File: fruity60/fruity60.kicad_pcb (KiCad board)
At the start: 2 copper layers, 126 parts

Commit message: progress
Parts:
- removed D0: D_Small, Diodes_SMD:D_SOD-123
- added De: D_Small, Diodes_SMD:D_SOD-123, F.Cu at (-67.5, 38.9)
- moved D1 7.94 mm to (-48.4, 38.9)
- moved D2 7.14 mm to (-29.4, 38.9)
- moved D3 7.14 mm to (-10.3, 38.9)
- moved D4 7.14 mm to (8.73, 38.9)
- moved D5 7.14 mm to (27.8, 38.9)
- moved D6 7.14 mm to (46.8, 38.9)
- moved D7 7.14 mm to (65.9, 38.9)
- moved D8 7.14 mm to (84.9, 38.9)
- moved D9 7.14 mm to (104.0, 38.9)
- moved DA1 7.14 mm to (123.0, 38.9)
- moved D10 5.62 mm to (-65.1, 42.1)
- moved D11 5.56 mm to (-46.0, 42.1)
- moved D12 5.56 mm to (-27.0, 42.1)
- moved D13 5.56 mm to (-7.94, 42.1)
- moved D14 5.56 mm to (11.1, 42.1)
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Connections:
- MX0A1 pad 1: B7 -> C7
- MX18 pad 1: C7 -> B7
- MX1A1 pad 1: B7 -> C7
- MX28 pad 1: C7 -> B7
- MX2A1 pad 1: B7 -> C7
- MX38 pad 1: C7 -> B7
- MX3A1 pad 1: B7 -> C7
- MX48 pad 1: C7 -> B7
- MX4A1 pad 1: B7 -> C7
- MX58 pad 1: C7 -> B7
- MX5A1 pad 1: B7 -> C7
- MX8 pad 1: C7 -> B7
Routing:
- net D3: track 197.3 -> 457.5 mm
- net D2: track 220.8 -> 438.2 mm
- net C6: track 239.4 -> 42.3 mm
- net F0: track 283.4 -> 464.0 mm
- net F1: track 277.0 -> 419.8 mm
- net Net-(D4A1-Pad2): track 0.00 -> 127.3 mm
- net Net-(D49-Pad2): track 0.00 -> 126.1 mm
- net Net-(D59-Pad2): track 0.00 -> 119.9 mm
- net Net-(D48-Pad2): track 0.00 -> 117.8 mm
- net Net-(D45-Pad2): track 0.00 -> 108.9 mm
- net Net-(D56-Pad2): track 0.00 -> 107.1 mm
- net Net-(D5A1-Pad2): track 0.00 -> 103.9 mm
- net Net-(D41-Pad2): track 0.00 -> 103.3 mm
- net F4: track 298.0 -> 400.2 mm
- net Net-(D42-Pad2): track 0.00 -> 95.5 mm
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
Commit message: 10 unconnected10 unconnected10 unconnected10 unconnected10 unconnected10 unconnected10 unconnected10 unconnected10 unconnected10 unconnected
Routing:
- net C6: track 42.3 -> 302.2 mm, vias 0 -> 11
- net D0: track 37.5 -> 257.8 mm, vias 0 -> 7
- net C7: track 151.6 -> 215.7 mm
- net D6: track 212.4 -> 233.1 mm
- net Net-(D45-Pad2): track 108.9 -> 94.8 mm
- net Net-(D57-Pad2): track 93.3 -> 79.2 mm
- net Net-(D35-Pad2): track 74.2 -> 76.1 mm
- net D7: track 301.4 -> 300.1 mm
- net F6: vias 2 -> 0

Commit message: Update with all nets
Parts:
- JP1: footprint Pin_Headers:Pin_Header_Straight_1x16_Pitch2.54mm -> Adafruit Feather 32u4 Bluefruit LE:1X16_ROUND
- JP2: footprint Pin_Headers:Pin_Header_Straight_1x12_Pitch2.54mm -> Adafruit Feather 32u4 Bluefruit LE:1X12_ROUND
- moved JP1 29.6 mm to (191.8, 25.4), turned to 0 degrees
- moved JP2 8.64 mm to (186.7, 45.7), turned to 180 degrees
- moved D1A1 8.59 mm to (132.6, 37.3)
- moved D49 8.59 mm to (120.7, 47.6)
- moved D50 8.59 mm to (144.5, 47.6)
- moved D51 8.59 mm to (146.8, 47.6)
- moved D54 8.59 mm to (154.0, 47.6)
- moved D55 8.59 mm to (156.4, 47.6)
- moved D56 8.59 mm to (158.8, 47.6)
- moved D59 8.59 mm to (165.9, 47.6)
- moved D5A1 8.59 mm to (168.3, 47.6)
- moved MX27 8.59 mm to (84.9, 98.4)
- moved MX2A1 8.59 mm to (142.1, 98.4)
- moved MX39 8.59 mm to (132.6, 117.5)
- moved MX50 8.59 mm to (146.8, 60.3)
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- renumbered De to D0
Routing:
- net D3: track 457.5 -> 610.9 mm, vias 0 -> 2
- net F1: track 419.8 -> 545.0 mm
- net B7: track 224.2 -> 334.0 mm, vias 0 -> 1
- net D2: track 438.2 -> 536.8 mm, vias 0 -> 2
- net F0: track 464.0 -> 552.2 mm
- net Net-(D58-Pad2): track 31.3 -> 118.5 mm, vias 1 -> 2
- net F6: track 395.1 -> 476.4 mm, vias 0 -> 1
- net F7: track 384.4 -> 445.4 mm
- net F4: track 400.2 -> 451.3 mm
- net F5: track 409.6 -> 428.9 mm, vias 0 -> 1

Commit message: first milestone
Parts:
- moved D0 98.0 mm to (-38.1, -61.3)
- moved D10 98.0 mm to (-35.7, -58.1)
- moved D12 98.0 mm to (2.38, -58.1)
- moved D14 98.0 mm to (40.5, -58.1)
- moved D15 98.0 mm to (59.5, -58.1)
- moved D18 98.0 mm to (116.7, -58.1)
- moved D2 98.0 mm to (0.00, -61.3)
- moved D20 98.0 mm to (-33.3, -54.9)
- moved D21 98.0 mm to (-14.3, -54.9)
- moved D23 98.0 mm to (23.8, -54.9)
- moved D25 98.0 mm to (61.9, -54.9)
- moved D26 98.0 mm to (81.0, -54.9)
- moved D27 98.0 mm to (100.0, -55.0)
- moved D29 98.0 mm to (138.1, -54.9)
- moved D3 98.0 mm to (19.1, -61.3)
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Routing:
- net F7: track 445.4 -> 482.3 mm, vias 0 -> 1
- net F5: track 428.9 -> 465.6 mm
- net F6: track 476.4 -> 496.4 mm
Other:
- board text added: "Fruity60"
- board text added: "prototype version 1"
- board text added: "yanfali (c) 2019"

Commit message: m2 holes
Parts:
- added REF**: MountingHole_2.2mm_M2, Mounting_Holes:MountingHole_2.2mm_M2, F.Cu at (151.1, 168.9)
- added REF**: MountingHole_2.2mm_M2, Mounting_Holes:MountingHole_2.2mm_M2, F.Cu at (151.1, 31.8)
- added REF**: MountingHole_2.2mm_M2, Mounting_Holes:MountingHole_2.2mm_M2, F.Cu at (8.89, 35.6)
- added REF**: MountingHole_2.2mm_M2, Mounting_Holes:MountingHole_2.2mm_M2, F.Cu at (6.35, 167.6)
- added REF**: MountingHole_2.2mm_M2, Mounting_Holes:MountingHole_2.2mm_M2, F.Cu at (295.9, 167.6)
- added REF**: MountingHole_2.2mm_M2, Mounting_Holes:MountingHole_2.2mm_M2, F.Cu at (295.9, 36.8)
- moved D17 126.1 mm to (156.1, 53.7)
- moved D19 126.1 mm to (194.2, 53.7)
- moved D38 126.1 mm to (179.9, 60.0)
- moved D3A1 126.1 mm to (218.0, 60.0)
- moved D51 126.1 mm to (227.5, 64.0)
- moved D52 126.1 mm to (229.9, 64.0)
- moved D56 126.1 mm to (239.4, 64.0)
- moved D57 126.1 mm to (241.8, 64.0)
- moved MX18 126.1 mm to (179.9, 95.7)
- moved MX1A1 126.1 mm to (218.0, 95.7)
- moved MX36 126.1 mm to (156.1, 133.8)
- moved MX38 126.1 mm to (194.2, 133.8)
- moved MX49 126.1 mm to (256.1, 152.9)
- moved MX4A1 126.1 mm to (279.9, 152.9)
- moved MX50 126.1 mm to (227.5, 76.7)
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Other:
- board text added: "prototype by yanfali (c) 2019"
- board text removed: "prototype version 1"
- board text removed: "yanfali (c) 2019"

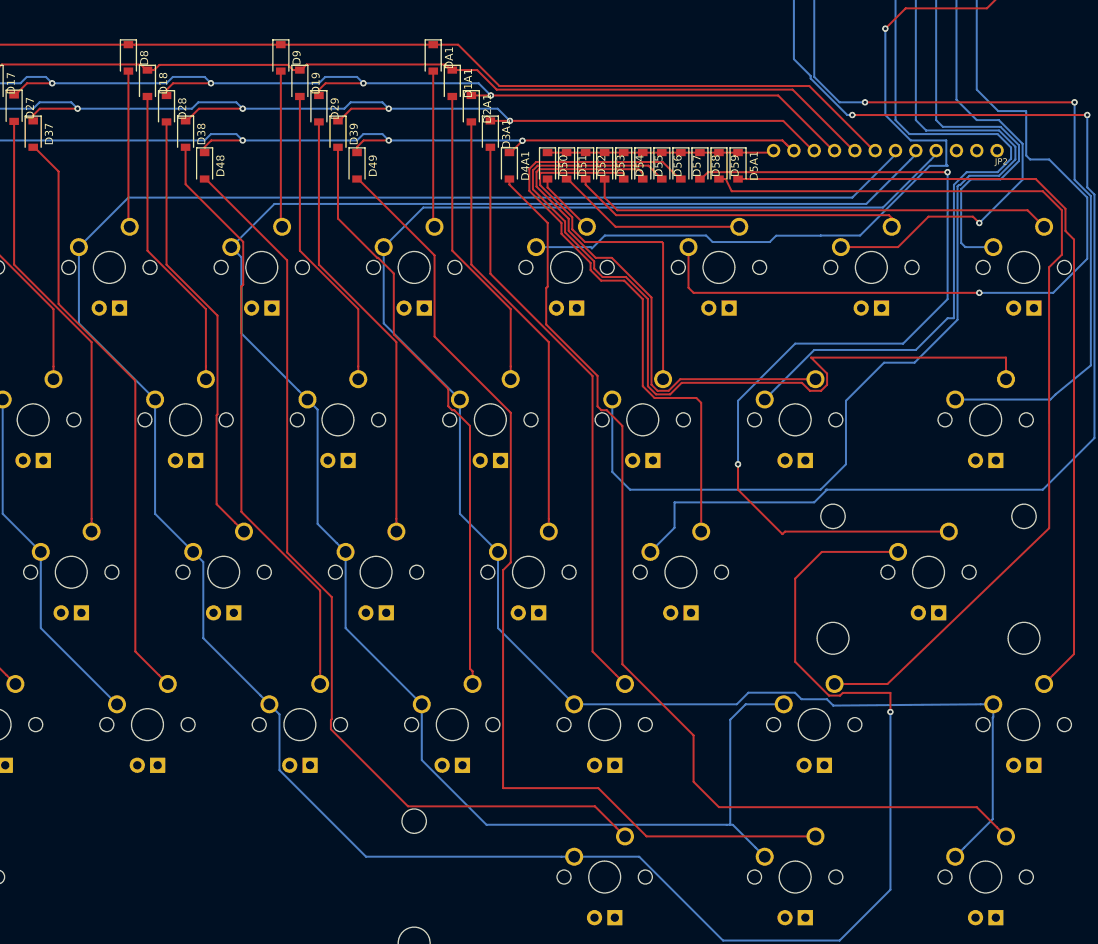
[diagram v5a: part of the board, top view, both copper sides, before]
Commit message: Add some silkscreen
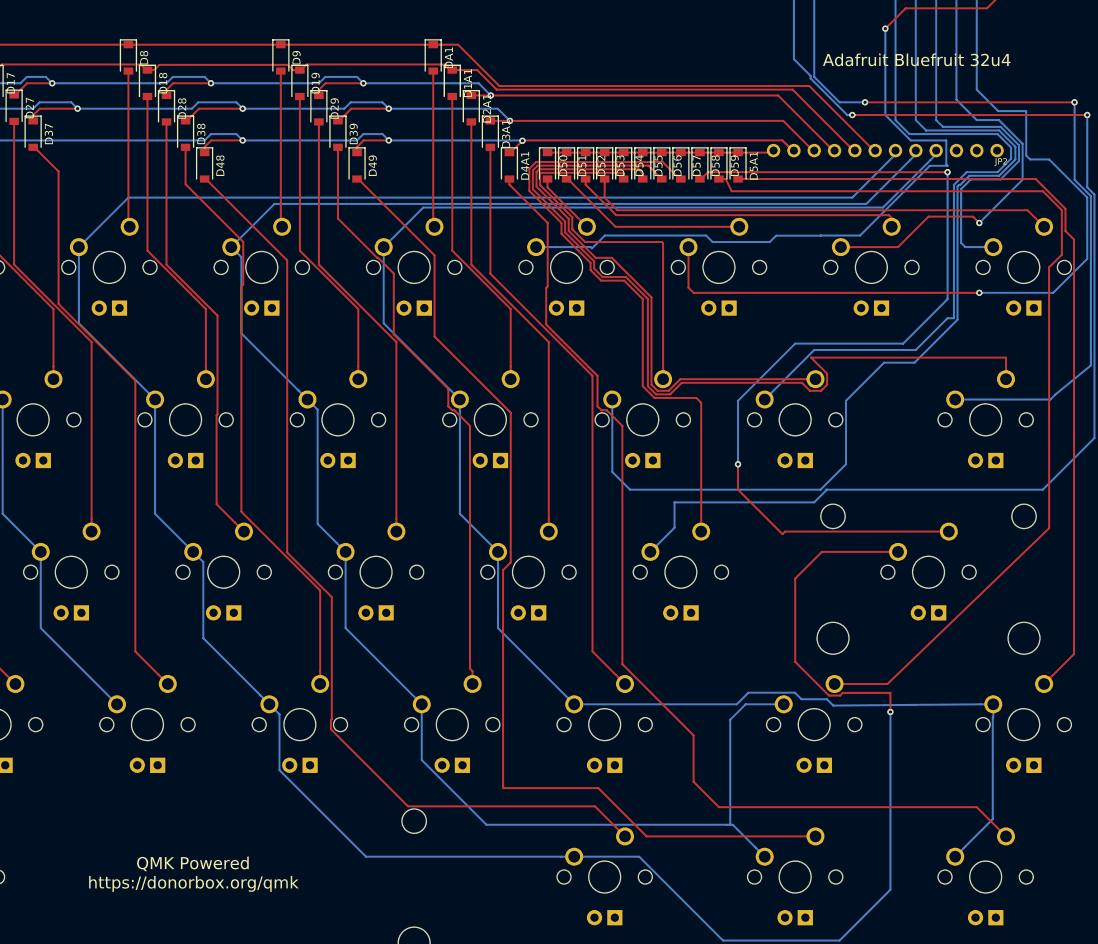
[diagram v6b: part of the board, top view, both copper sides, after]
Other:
- board text added: "Adafruit Bluefruit 32u4"
- board text added: "QMK Powered https://donorbox.org/qmk"
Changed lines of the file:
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@@
   (general
     (thickness 1.6)
-    (drawings 10)
+    (drawings 12)
     (tracks 1077)
     (zones 0)
@@
     (46 B.CrtYd user)
     (47 F.CrtYd user)
-    (48 B.Fab user hide)
+    (48 B.Fab user)
     (49 F.Fab user hide)
   )
@@
     )
   )
+  (gr_text "QMK Powered\nhttps://donorbox.org/qmk" (at 180.81625 152.4) (layer F.SilkS)
+    (effects (font (size 1.5 1.5) (thickness 0.15)))
+  )
+  (gr_text "Adafruit Bluefruit 32u4" (at 271.30375 50.8) (layer F.SilkS)
+    (effects (font (size 1.5 1.5) (thickness 0.15)))
+  )
   (gr_text "prototype by yanfali (c) 2019" (at 120.65 157.48) (layer F.SilkS)

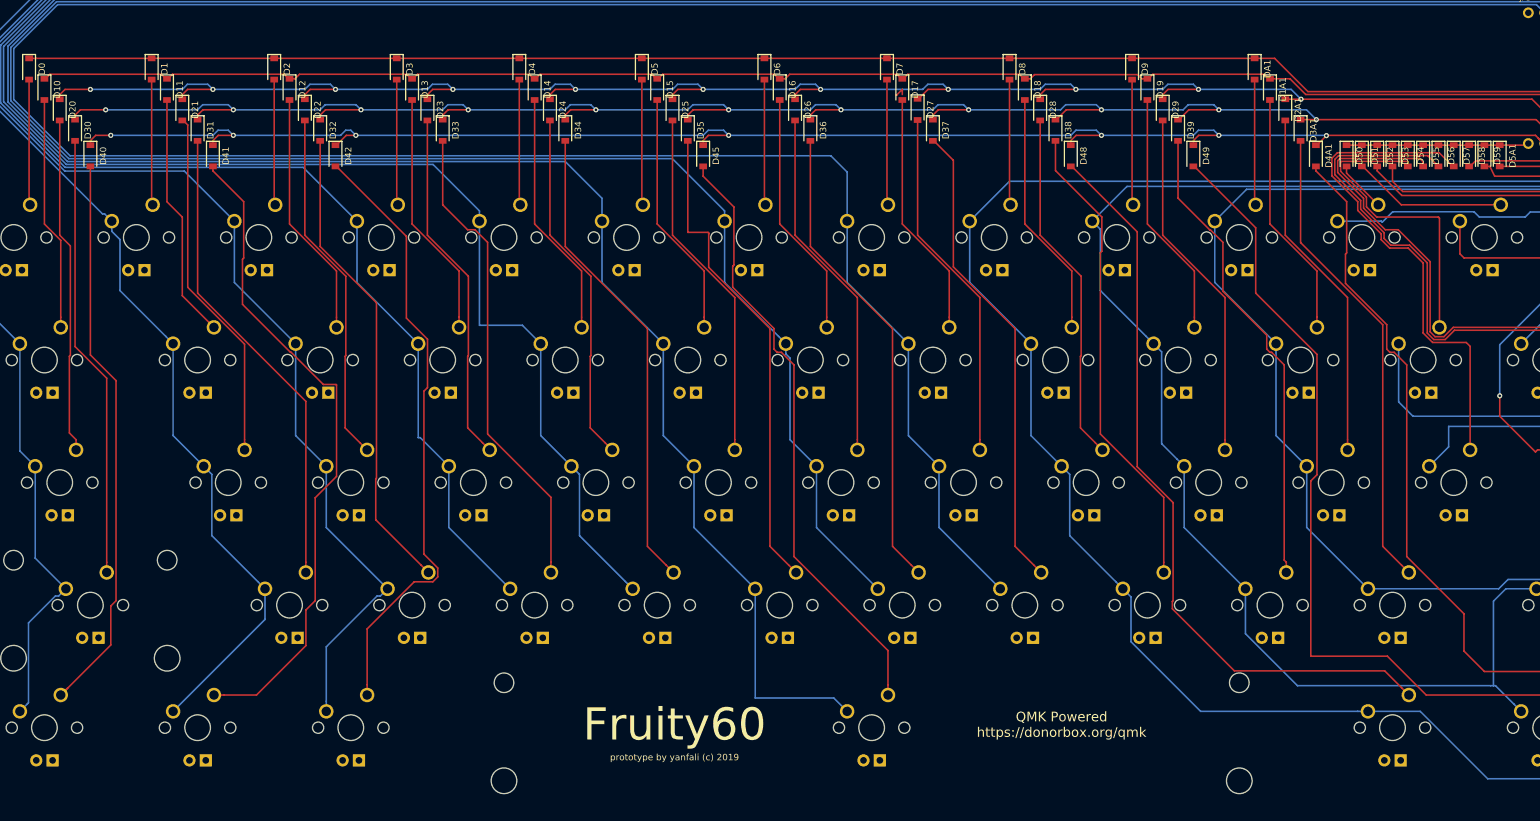
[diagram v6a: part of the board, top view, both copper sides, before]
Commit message: silkscreen additions
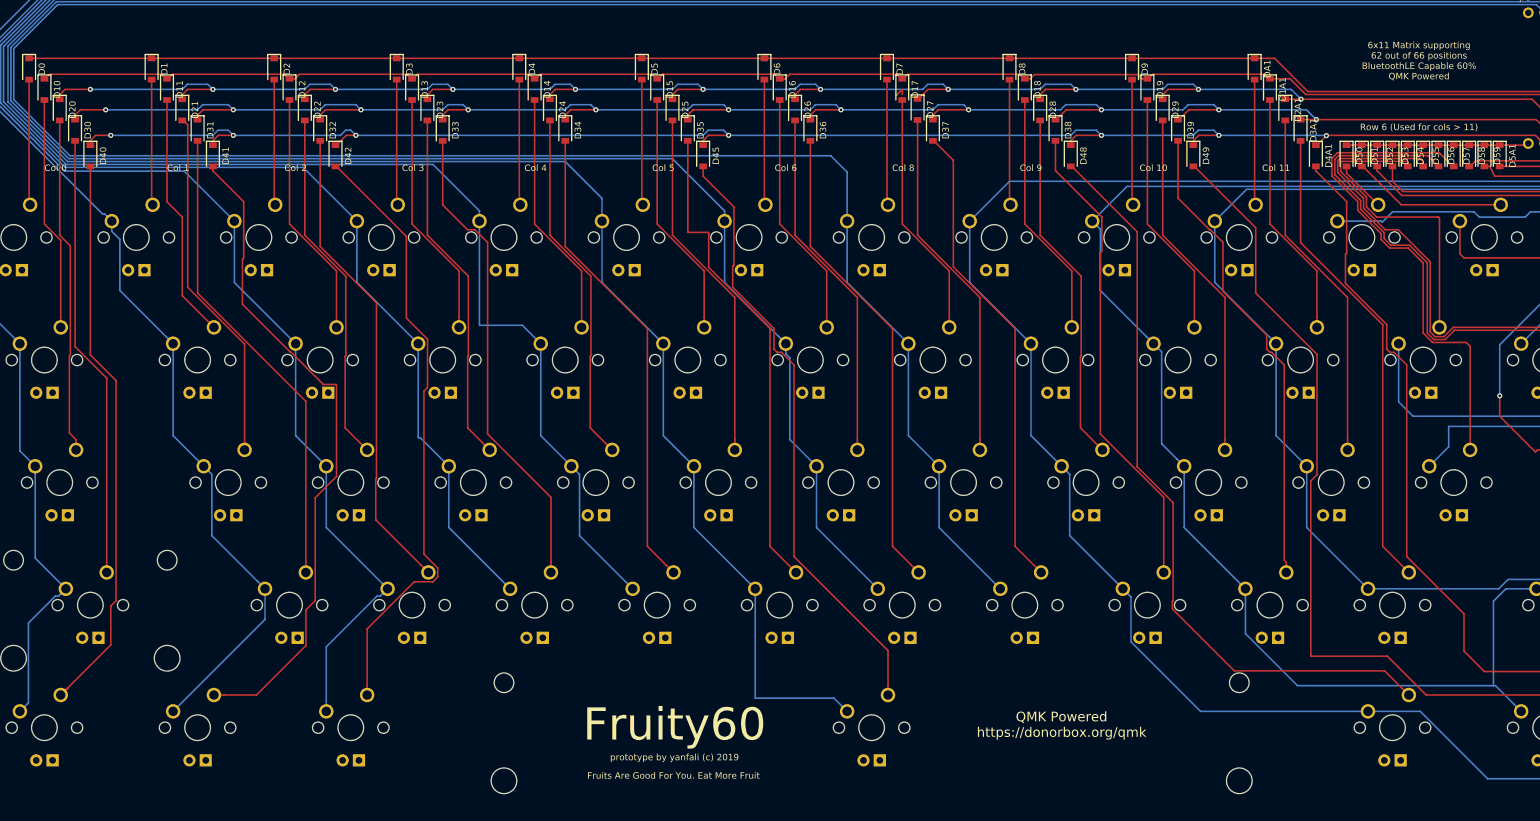
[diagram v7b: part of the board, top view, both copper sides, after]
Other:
- board text added: "6x11 Matrix supporting 62 out of 66 positions BluetoothLE Capable 60% QMK Powered"
- board text added: "Col 0"
- board text added: "Col 1"
- board text added: "Col 10"
- board text added: "Col 11"
- board text added: "Col 2"
- board text added: "Col 3"
- board text added: "Col 4"
- board text added: "Col 5"
- board text added: "Col 6"
- board text added: "Col 8"
- board text added: "Col 9"
- board text added: "Fruits Are Good For You. Eat More Fruit"
- board text added: "Row 6 (Used for cols > 11)"
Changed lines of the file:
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@@
   (general
     (thickness 1.6)
-    (drawings 12)
+    (drawings 26)
     (tracks 1077)
     (zones 0)
@@
   (page A4)
   (layers
-    (0 F.Cu signal)
-    (31 B.Cu signal)
+    (0 F.Cu signal hide)
+    (31 B.Cu signal hide)
     (32 B.Adhes user)
     (33 F.Adhes user)
@@
     )
   )
+  (gr_text "6x11 Matrix supporting\n62 out of 66 positions\nBluetoothLE Capable 60%\nQMK Powered" (at 236.37875 49.2125) (layer F.SilkS)
+    (effects (font (size 1 1) (thickness 0.15)))
+  )
+  (gr_text "Fruits Are Good For You. Eat More Fruit" (at 120.49125 160.3375) (layer F.SilkS)
+    (effects (font (size 1 1) (thickness 0.15)))
+  )
+  (gr_text "Row 6 (Used for cols > 11)" (at 236.37875 59.53125) (layer F.SilkS)
+    (effects (font (size 1 1) (thickness 0.15)))
+  )
+  (gr_text "Col 11" (at 214.15375 65.88125) (layer F.SilkS)
+    (effects (font (size 1 1) (thickness 0.15)))
+  )
+  (gr_text "Col 10" (at 195.10375 65.88125) (layer F.SilkS)
+    (effects (font (size 1 1) (thickness 0.15)))
+  )
+  (gr_text "Col 9" (at 176.05375 65.88125) (layer F.SilkS)
+    (effects (font (size 1 1) (thickness 0.15)))
+  )
+  (gr_text "Col 8" (at 156.21 65.88125) (layer F.SilkS)
+    (effects (font (size 1 1) (thickness 0.15)))
+  )
+  (gr_text "Col 6" (at 137.95375 65.88125) (layer F.SilkS)
+    (effects (font (size 1 1) (thickness 0.15)))
+  )
+  (gr_text "Col 5" (at 118.90375 65.88125) (layer F.SilkS)
+    (effects (font (size 1 1) (thickness 0.15)))
+  )
+  (gr_text "Col 4" (at 99.06 65.88125) (layer F.SilkS)
+    (effects (font (size 1 1) (thickness 0.15)))
+  )
+  (gr_text "Col 3" (at 80.01 65.88125) (layer F.SilkS)
+    (effects (font (size 1 1) (thickness 0.15)))
+  )
+  (gr_text "Col 1" (at 43.4975 65.88125) (layer F.SilkS)
+    (effects (font (size 1 1) (thickness 0.15)))
+  )
+  (gr_text "Col 0" (at 24.4475 65.88125) (layer F.SilkS)
+    (effects (font (size 1 1) (thickness 0.15)))
+  )
+  (gr_text "Col 2" (at 61.75375 65.88125) (layer F.SilkS)
+    (effects (font (size 1 1) (thickness 0.15)))
+  )
   (gr_text "QMK Powered\nhttps://donorbox.org/qmk" (at 180.81625 152.4) (layer F.SilkS)

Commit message: Add matrix labels to switch positions
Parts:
- MX0: value MX-NoLED -> K00
- MX0A1: value MX-NoLED -> K0A
- MX1: value MX-NoLED -> K01
- MX10: value MX-NoLED -> K10
- MX11: value MX-NoLED -> K11
- MX12: value MX-NoLED -> K12
- MX13: value MX-NoLED -> K13
- MX14: value MX-NoLED -> K14
- MX15: value MX-NoLED -> K15
- MX16: value MX-NoLED -> K16
- MX17: value MX-NoLED -> K17
- MX18: value MX-NoLED -> K18
- MX19: value MX-NoLED -> K19
- MX1A1: value MX-NoLED -> K1A
- MX2: value MX-NoLED -> K02
- MX20: value MX-NoLED -> K20
- MX21: value MX-NoLED -> K21
- MX22: value MX-NoLED -> K22
- MX23: value MX-NoLED -> K23
- MX24: value MX-NoLED -> K24
- MX25: value MX-NoLED -> K25
- MX26: value MX-NoLED -> K26
- MX27: value MX-NoLED -> K27
- MX28: value MX-NoLED -> K28
- MX29: value MX-NoLED -> K29
- MX2A1: value MX-NoLED -> K2A
- MX3: value MX-NoLED -> K03
- MX30: value MX-NoLED -> K30
- MX31: value MX-NoLED -> K31
- MX32: value MX-NoLED -> K32
- MX33: value MX-NoLED -> K33
- MX34: value MX-NoLED -> K34
- MX35: value MX-NoLED -> K35
- MX36: value MX-NoLED -> K36
- MX37: value MX-NoLED -> K37
- MX38: value MX-NoLED -> K38
- MX39: value MX-NoLED -> K39
- MX3A1: value MX-NoLED -> K3A
- MX4: value MX-NoLED -> K04
- MX40: value MX-NoLED -> K40
- MX41: value MX-NoLED -> K41
- MX42: value MX-NoLED -> K42
- MX45: value MX-NoLED -> K45
- MX48: value MX-NoLED -> K48
- MX49: value MX-NoLED -> K49
- MX4A1: value MX-NoLED -> K4A
- MX5: value MX-NoLED -> K05
- MX50: value MX-NoLED -> K50
- MX51: value MX-NoLED -> K51
- MX52: value MX-NoLED -> K52
- MX53: value MX-NoLED -> K53
- MX54: value MX-NoLED -> K54
- MX55: value MX-NoLED -> K55
- MX56: value MX-NoLED -> K56
- MX57: value MX-NoLED -> K57
- MX58: value MX-NoLED -> K58
- MX59: value MX-NoLED -> K59
- MX5A1: value MX-NoLED -> K5A
- MX6: value MX-NoLED -> K06
- MX7: value MX-NoLED -> K07
- MX8: value MX-NoLED -> K08
- MX9: value MX-NoLED -> K09
